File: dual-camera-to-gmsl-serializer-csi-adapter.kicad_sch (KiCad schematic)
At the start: 118 parts, among them J1 Conn_FFC_WE_68715014022, J2 Conn_FFC_WE_68715014022, J3 Conn_FFC_WE_68715014022, U1 TPS2117DRLR, U2 TPS2117DRLR, U3 AP62301_TSOT

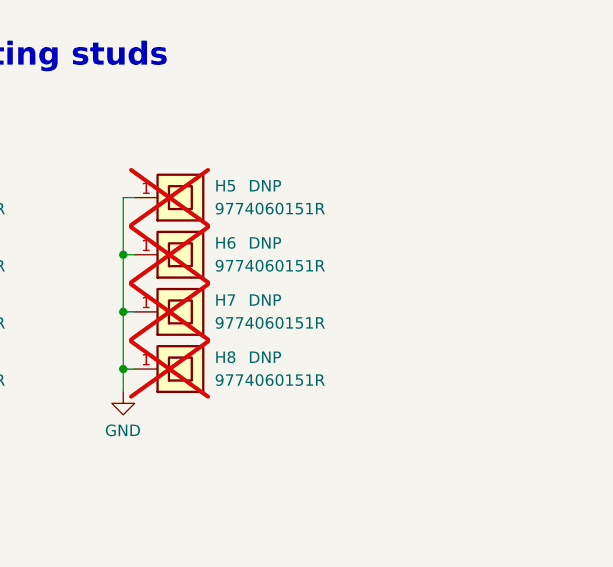
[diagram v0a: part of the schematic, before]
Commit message: [#70359] PCB: Align spacers with camera board
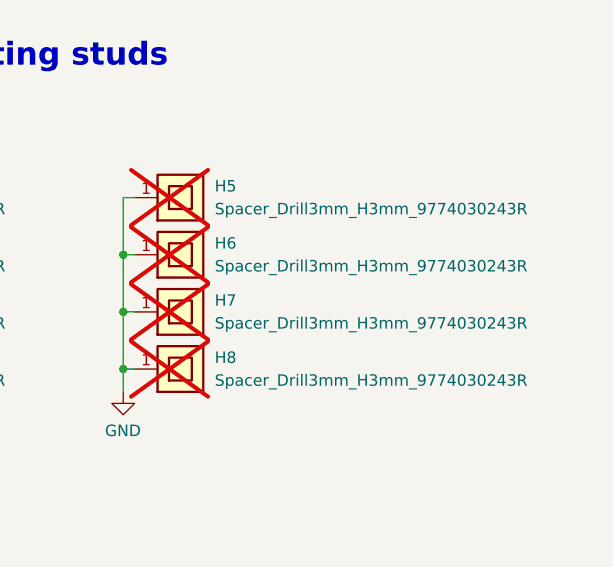
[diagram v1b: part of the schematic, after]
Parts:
- removed H5, H6, H7, H8: Spacer_Drill3.7mm_H6mm_9774060151R, antmicro-footprints:Spacer_Drill3.7mm_H6mm_9774060151R, symbol antmicroMechanicalParts:Spacer_Drill3.7mm_H6mm_9774060151R
- added H5, H6, H7, H8: Spacer_Drill3mm_H3mm_9774030243R, antmicro-footprints:Spacer_Drill3mm_H3mm_9774030243R, symbol antmicroMechanicalParts:Spacer_Drill3mm_H3mm_9774030243R
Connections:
- net GND: now also H5.1, H6.1, H7.1, H8.1

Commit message: [#70359] Add TODOs after first review
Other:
- note added: "CAM1"
- note added: "CAM2"
- note added: "TODO: Add OSHW and Antmicro logos to the schematics"
- note added: "TODO: Add QWIC connectors for I2C exposed from every serializer This will allow to add more sensors and stream sensor data over GMSL"
- note added: "TODO: Default I2C-CSI naming/mapping to CSI is reversed"
- note added: "TODO: GPIO 4 named the same for both serializers It should probably be named differently"
- note added: "To camera 1"
- note added: "To camera 2"
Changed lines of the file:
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@@
 		)
 	)
+	(polyline
+		(pts
+			(xy 86.36 143.51) (xy 86.36 148.59)
+		)
+		(stroke
+			(width 0)
+			(type dash)
+		)
+	)
 	(wire
 		(pts
@@
 		)
 	)
+	(polyline
+		(pts
+			(xy 82.55 138.43) (xy 82.55 143.51)
+		)
+		(stroke
+			(width 0)
+			(type dash)
+		)
+	)
 	(bus
 		(pts
@@
 		)
 	)
+	(polyline
+		(pts
+			(xy 40.64 86.36) (xy 40.64 105.41)
+		)
+		(stroke
+			(width 0)
+			(type dash)
+		)
+	)
 	(bus
 		(pts
@@
 		)
 	)
+	(polyline
+		(pts
+			(xy 40.64 43.18) (xy 40.64 69.85)
+		)
+		(stroke
+			(width 0)
+			(type dash)
+		)
+	)
 	(wire
 		(pts
@@
 		)
 	)
+	(text "TODO:\nGPIO 4 named the same for both serializers\nIt should probably be named differently"
+		(exclude_from_sim no)
+		(at 335.788 115.316 0)
+		(effects
+			(font
+				(size 1.27 1.27)
+			)
+		)
+	)
+	(text "CAM1"
+		(exclude_from_sim no)
+		(at 85.09 148.59 90)
+		(effects
+			(font
+				(size 1.27 1.27)
+			)
+			(justify left bottom)
+		)
+	)
 	(text "Power Status LEDs"
 		(exclude_from_sim no)
@@
 		)
 	)
+	(text "To camera 1"
+		(exclude_from_sim no)
+		(at 39.37 104.14 90)
+		(effects
+			(font
+				(size 1.6 1.6)
+			)
+			(justify left bottom)
+		)
+	)
+	(text "TODO:\nAdd QWIC connectors for I2C exposed from every serializer\nThis will allow to add more sensors and stream sensor data over GMSL"
+		(exclude_from_sim no)
+		(at 188.722 156.21 0)
+		(effects
+			(font
+				(size 1.27 1.27)
+			)
+			(justify left)
+		)
+	)
 	(text "Power Arbiters"
 		(exclude_from_sim no)
@@
 		)
 	)
+	(text "TODO:\nDefault I2C-CSI naming/mapping to CSI is reversed"
+		(exclude_from_sim no)
+		(at 65.024 135.636 0)
+		(effects
+			(font
+				(size 1.27 1.27)
+			)
+			(justify left)
+		)
+	)
 	(text "GMSL Serializer Board\nConnector 1"
 		(exclude_from_sim no)
@@
 		)
 	)
+	(text "CAM2"
+		(exclude_from_sim no)
+		(at 81.28 143.51 90)
+		(effects
+			(font
+				(size 1.27 1.27)
+			)
+			(justify left bottom)
+		)
+	)
+	(text "TODO:\nAdd OSHW and Antmicro logos to the schematics"
+		(exclude_from_sim no)
+		(at 102.87 276.352 0)
+		(effects
+			(font
+				(size 1.27 1.27)
+			)
+			(justify left)
+		)
+	)
 	(text "GMSL Serializer Board\nConnector 2"
 		(exclude_from_sim no)
@@
 		)
 	)
+	(text "To camera 2"
+		(exclude_from_sim no)
+		(at 38.608 64.77 90)
+		(effects
+			(font
+				(size 1.6 1.6)
+			)
+			(justify left bottom)
+		)
+	)
 	(label "FB_3V3"
 		(at 157.48 243.84 0)
@@
 		(dnp no)
 		(property "Reference" "J1"
-			(at 44.45 108.585 0)
+			(at 48.26 38.354 0)
 			(effects
 				(font
@@
 		)
 		(property "MPN" "68715014022"
-			(at 44.45 111.125 0)
+			(at 58.928 40.386 0)
 			(effects
 				(font

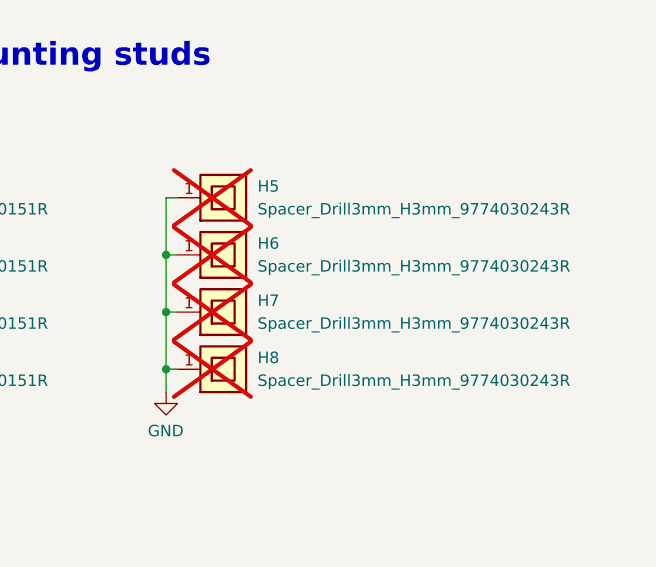
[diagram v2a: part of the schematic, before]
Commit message: [#70359] PCB: Update OV5640 mounting holes
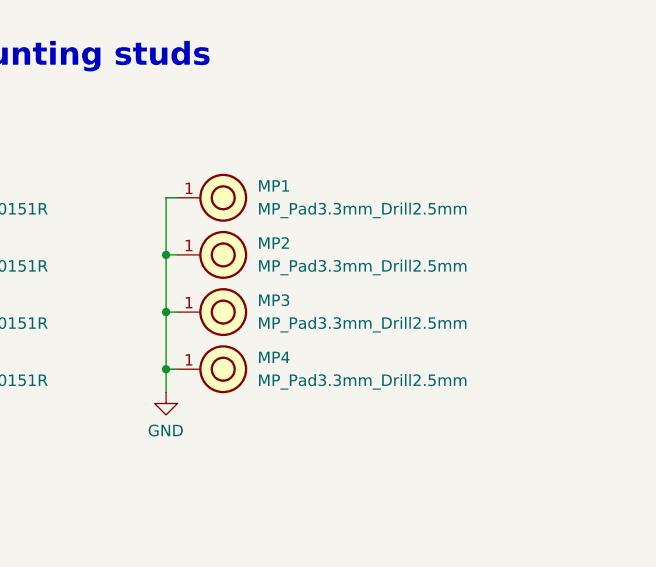
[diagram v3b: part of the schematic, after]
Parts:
- removed H5, H6, H7, H8: Spacer_Drill3mm_H3mm_9774030243R, antmicro-footprints:Spacer_Drill3mm_H3mm_9774030243R, symbol antmicroMechanicalParts:Spacer_Drill3mm_H3mm_9774030243R
- added MP1, MP2, MP3, MP4: MP_Pad3.3mm_Drill2.5mm, antmicro-footprints:MP_Pad3.3mm_Drill2.5mm, symbol antmicroMechanicalParts:MP_Pad3.3mm_Drill2.5mm
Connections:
- net GND: now also MP1.1, MP2.1, MP3.1, MP4.1

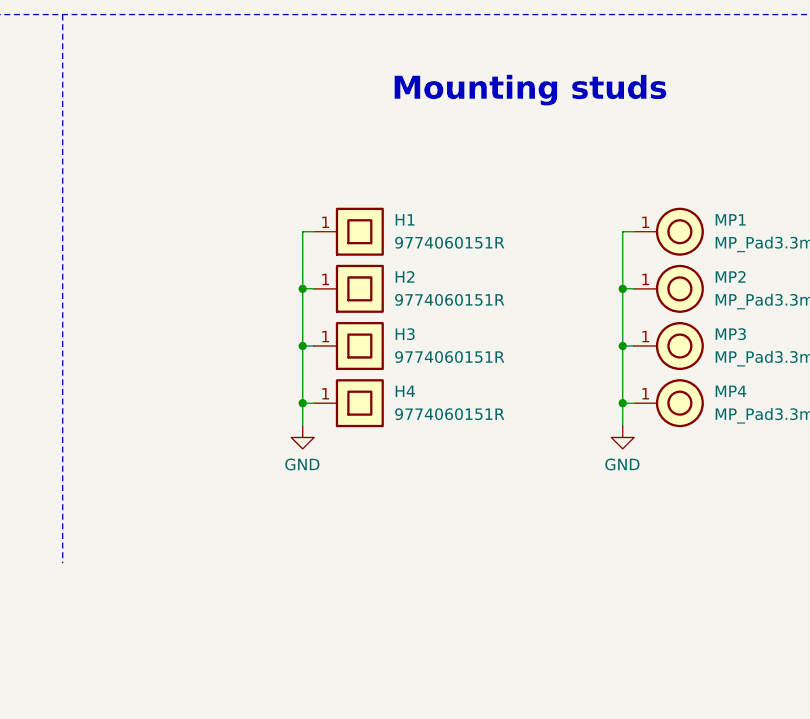
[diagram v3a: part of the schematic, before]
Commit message: [#70359] PCB: Add fastening holes
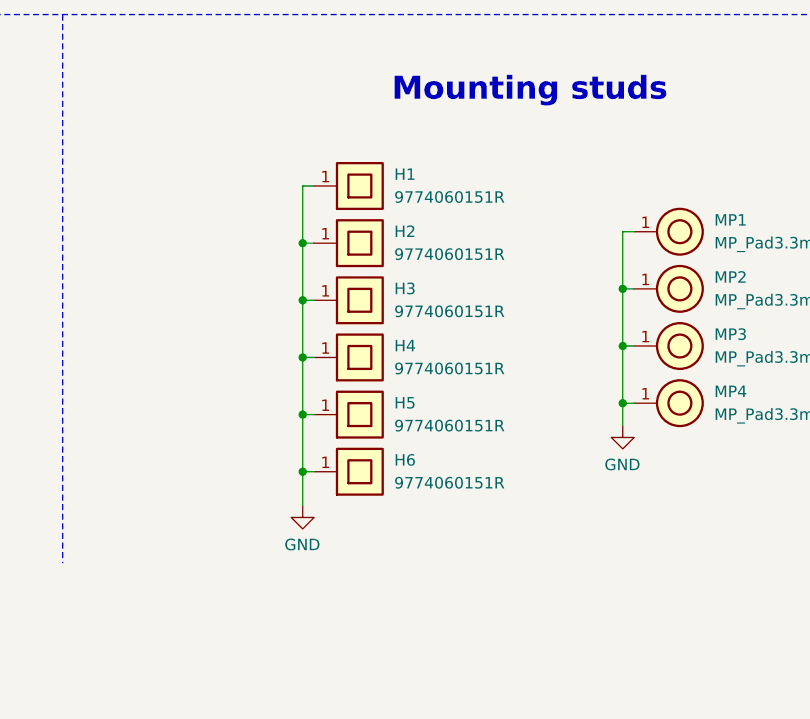
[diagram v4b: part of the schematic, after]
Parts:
- added H5, H6: Spacer_Drill3.7mm_H6mm_9774060151R, antmicro-footprints:Spacer_Drill3.7mm_H6mm_9774060151R, symbol antmicroMechanicalParts:Spacer_Drill3.7mm_H6mm_9774060151R
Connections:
- net GND: now also H5.1, H6.1
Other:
- moved on the sheet: H1, H2, H3, H4

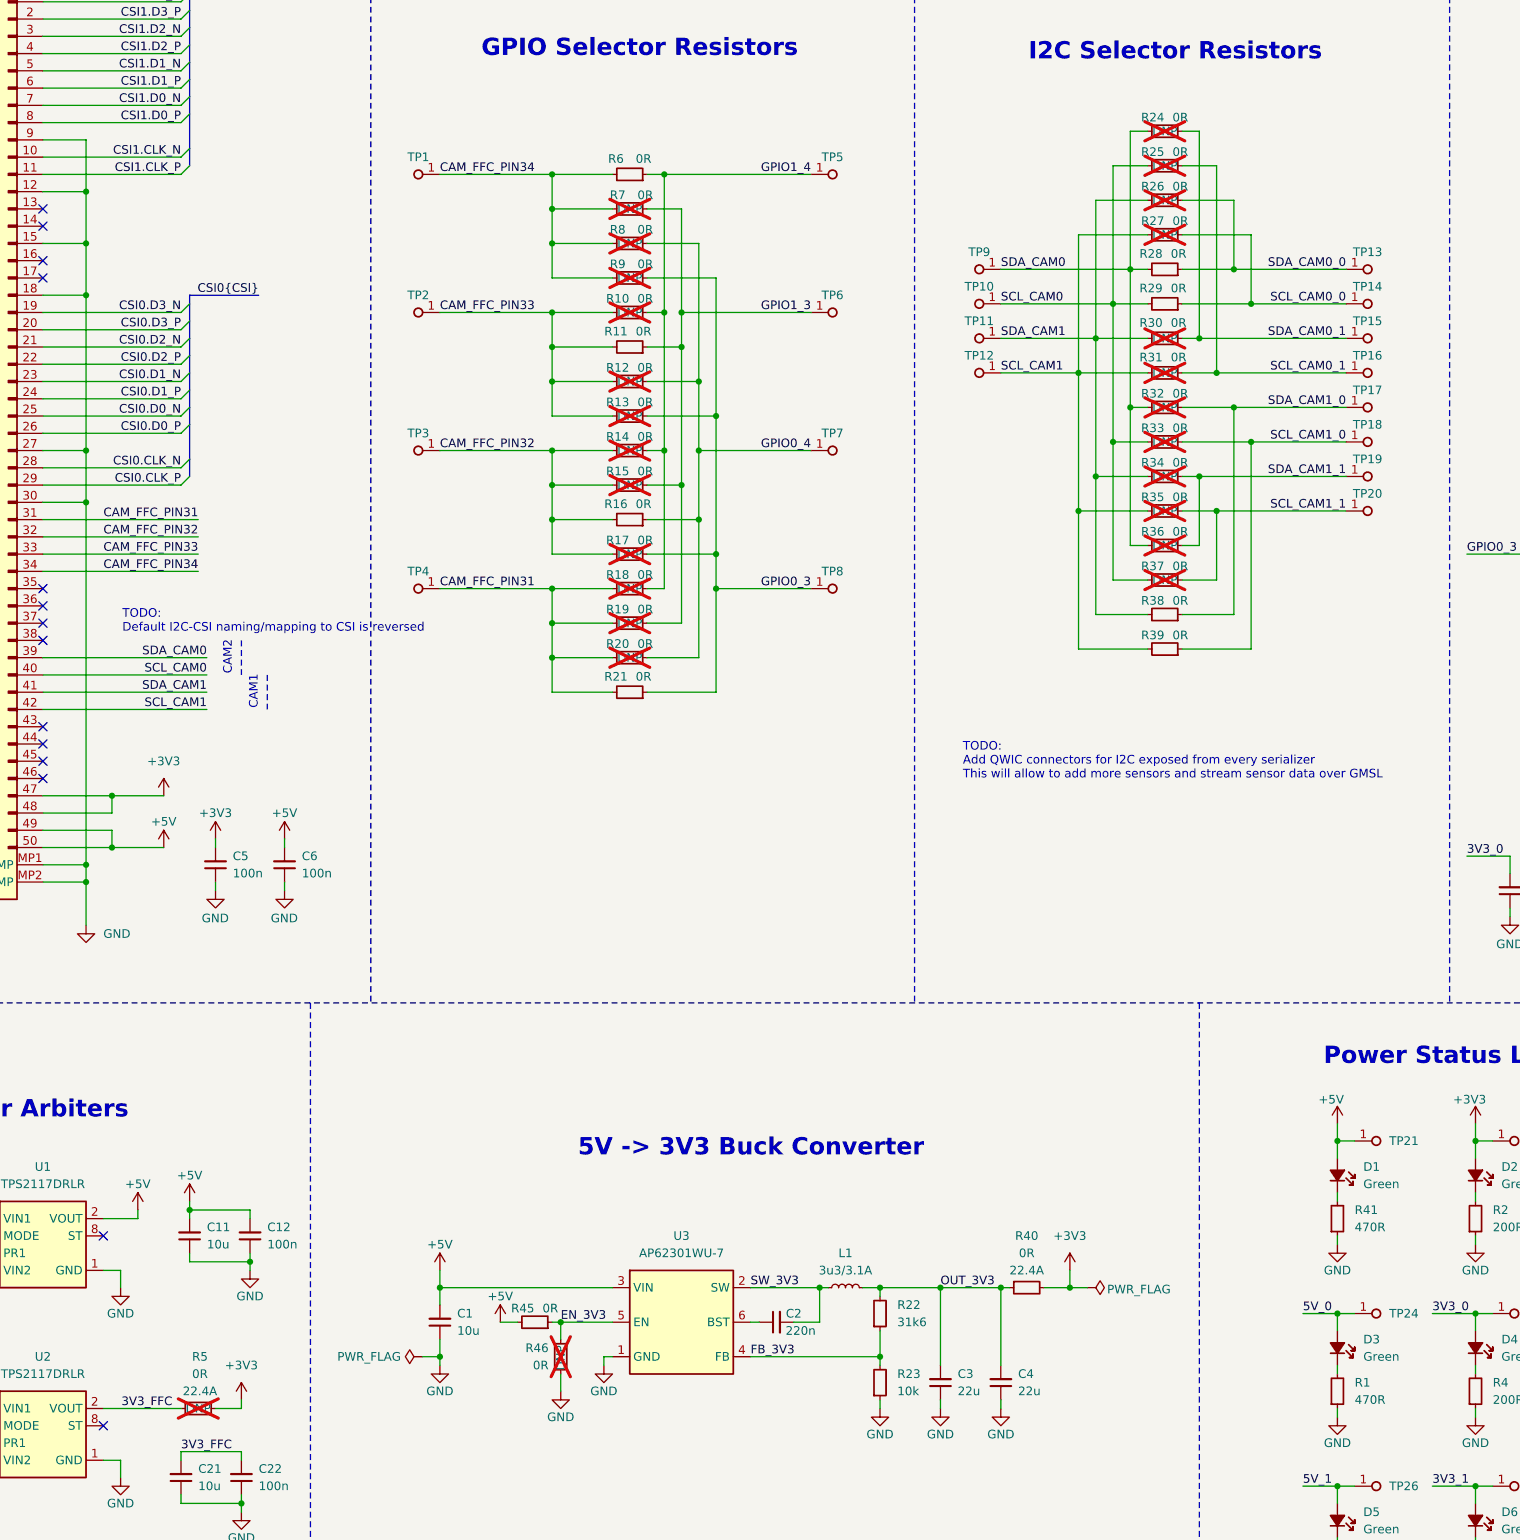
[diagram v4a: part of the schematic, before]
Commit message: [#70359] Schematic: Resolve I2C mapping
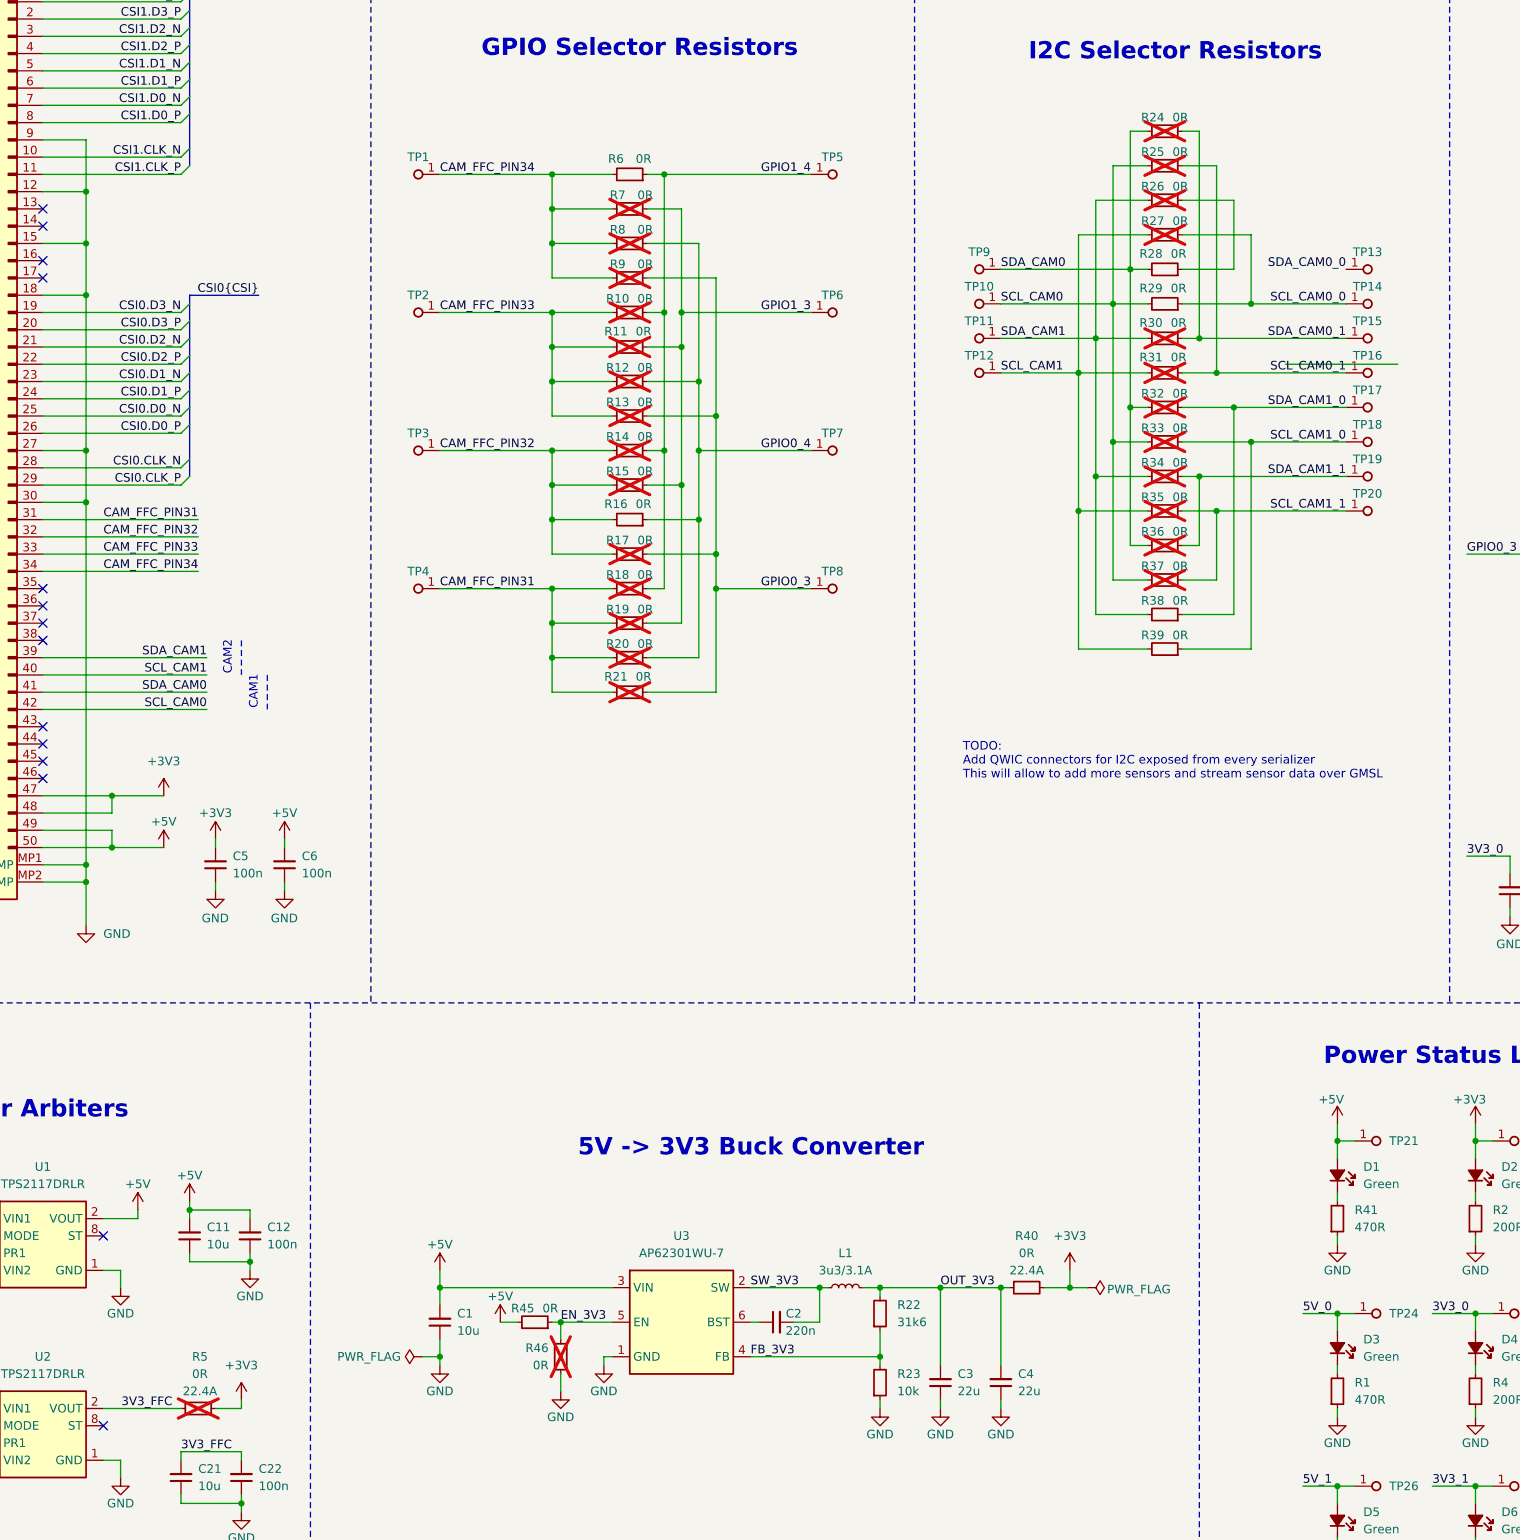
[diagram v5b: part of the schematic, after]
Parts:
- R10, R12, R13, R14, R15, R17, R18, R19, R20, R24, R25, R26, R27, R30, R31, R32, R33, R34, R35, R36, R37, R46, R5, R7, R8, R9: DNP DNP -> (none)
- R11, R21: now not fitted; now left out of the parts list
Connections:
- net SCL_CAM0: now also J1.42; no longer J1.40
- net SCL_CAM1: now also J1.40; no longer J1.42
- net SDA_CAM0: now also J1.41; no longer J1.39
- net SDA_CAM0_0: no longer R26.1, R28.1
- net SDA_CAM1: now also J1.39; no longer J1.41
- new net: R26.1, R28.1
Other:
- note removed: "TODO: Default I2C-CSI naming/mapping to CSI is reversed"
